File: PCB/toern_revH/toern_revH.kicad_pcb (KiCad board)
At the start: 4 copper layers, 160 x 71 mm, 118 parts, among them IC1 BQ24075TRGTR, J1 AudioJack3_Switch, J10 Conn_01x02, J11 Conn_01x05, J11.5 Conn_01x05, J12 Conn_01x05, J13 Conn_01x05, J14 Conn_01x05, J15 Conn_01x05, J16 Conn_01x02, J17 AudioJack3_Ground, J18 Conn_01x05_Socket, J19 Conn_01x05_Socket, J2 Conn_01x05_Socket, J20 Conn_01x05_Socket, J21 Conn_01x05_Socket, J22 Conn_01x05_Socket, J23 Conn_01x05_Socket, J24 Conn_01x05_Socket, J25 Conn_01x02, J26 Conn_01x02, J3 AudioJack3_Ground, J4 USB_C_Receptacle_USB2.0, J5 AudioJack3_Switch, J6 AudioJack3_Switch, J7 AudioJack3_Switch, J8 Micro_SD_Card, J9 Conn_01x03, U1 SPX3819M5-L-3-3, U13 PAM8403D, U14 74LVC1G17, U15 74AHCT1G125, U2 SPX3819M5-L-1-8, U3 SGTL5000XNBA3, U4 TLP2361V4_E, U5 74LVC2G14, U6 Teensy4.1, U7 SPX3819M5-L-3-3, U8 TPS22918DBVR

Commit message: fixed production files for revH
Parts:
- C32: value 10uF -> 10u
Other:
- board text added: "made in st.pauli by warft_labs V3.0 - 08/26 www.toern.live"
- board text removed: "made in st.pauli by warft_labs V2.1 - 05/26 www.toern.live"

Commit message: added protection for 5-12v clock input as well as 2nd clockout
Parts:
- removed MountingHole5: MountingHole_2.2mm_M2, MountingHole:MountingHole_2.2mm_M2
- added C39: 100nF, Capacitor_SMD:C_0402_1005Metric, F.Cu at (169.1, 37.1)
- added D2: D_Schottky_Dual_Series_ACK, Package_TO_SOT_SMD:SOT-23, F.Cu at (163.3, 30.3)
- added J27: Conn_01x02, Connector_JST:JST_PH_B2B-PH-K_1x02_P2.00mm_Vertical, F.Cu at (185.2, 68.2)
- added R31: 100k, Resistor_SMD:R_0402_1005Metric, F.Cu at (163.3, 38.8)
- added R32: 1k, Resistor_SMD:R_0402_1005Metric, F.Cu at (168.9, 39.4)
- added U16: 74AHCT1G125, Package_TO_SOT_SMD:SOT-23-5, F.Cu at (166.0, 38.9)
- R30: value 10k -> 22k
- moved R29 4.21 mm to (166.6, 31.2), turned to 0 degrees
- moved R30 4.11 mm to (166.5, 29.4), turned to 0 degrees
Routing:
- net Net-(J27-Pin_1): track 0.00 -> 42.2 mm, vias 0 -> 2
- net GND: track 159.9 -> 175.6 mm, vias 165 -> 172
- net 38_CS1_IN1: track 7.12 -> 17.9 mm
- net 35_TX8: track 41.8 -> 50.6 mm, vias 0 -> 2
- net Net-(D2-common): track 5.36 -> 13.0 mm
- net 28_RX7: track 0.00 -> 5.12 mm
- net 41_A17: track 68.5 -> 73.4 mm
- net +5V: track 415.6 -> 419.4 mm, vias 3 -> 4
- net 37_CS: track 20.6 -> 23.5 mm
- net +3.3V: track 375.9 -> 378.6 mm, vias 15 -> 17
- net Net-(R32-Pad2): track 0.00 -> 2.17 mm
- net 34_RX8: track 30.1 -> 31.0 mm
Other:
- board text added: "+ -"
- board text added: "SIDEC-5V"

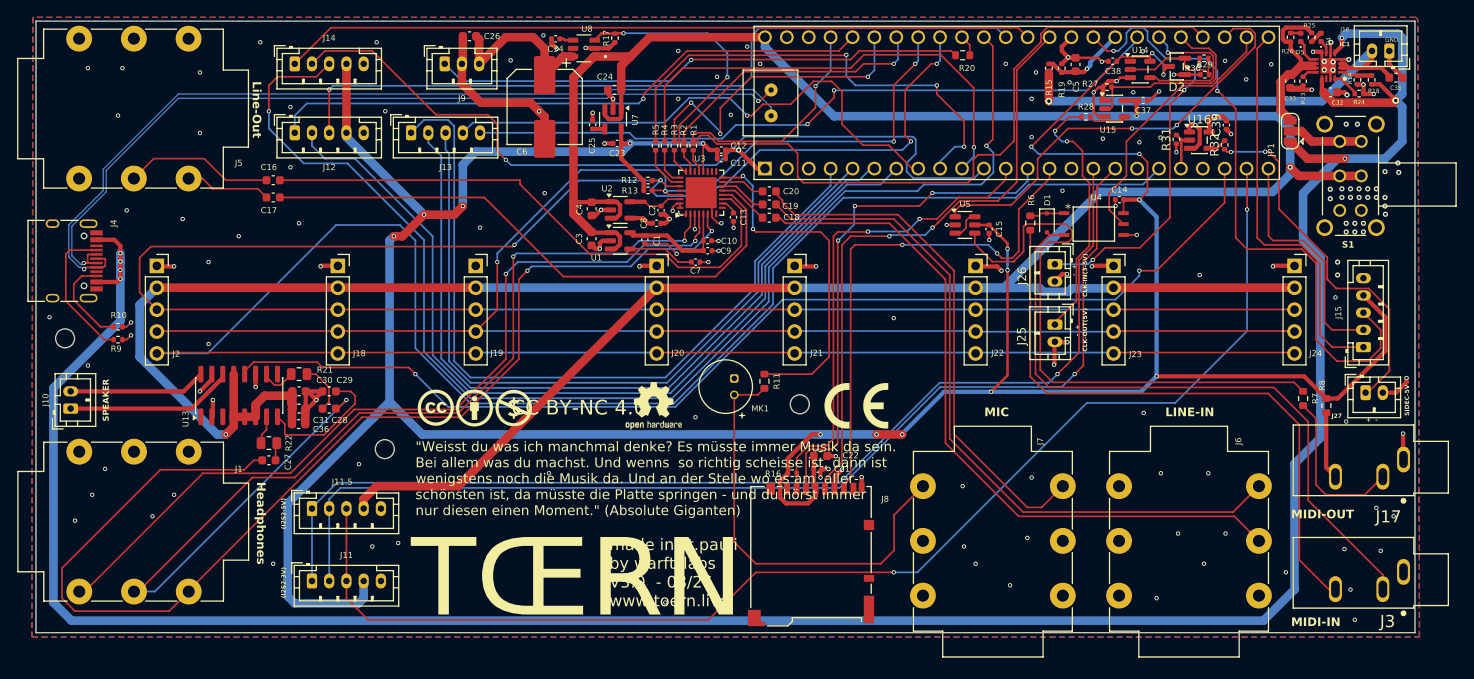
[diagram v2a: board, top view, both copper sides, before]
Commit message: added pogo pins and connectors to pcv revH
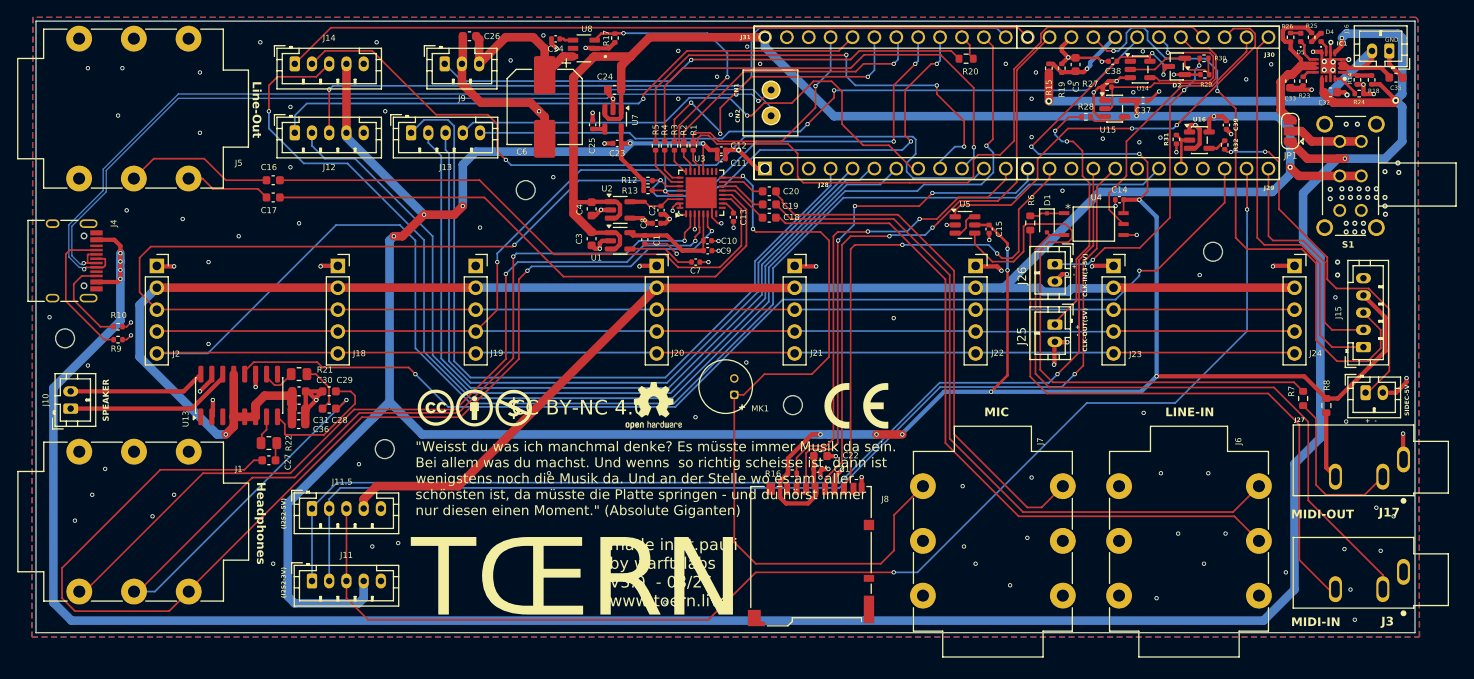
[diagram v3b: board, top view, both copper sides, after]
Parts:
- removed R11: 2.2k, Resistor_SMD:R_0603_1608Metric
- added CN1: YZP0354-20100-01, YZP0354-20100-01:YZP0354-20100-01, F.Cu at (116.3, 33.0)
- added CN2: YZP0354-20100-01, YZP0354-20100-01:YZP0354-20100-01, F.Cu at (116.3, 36.0)
- added J28: 929870-01-12-RA, 3M_929870-01-12-RA:3M_929870-01-12-RA_Assembly, F.Cu at (129.5, 42.1)
- added J29: 929870-01-12-RA, 3M_929870-01-12-RA:3M_929870-01-12-RA_Assembly, F.Cu at (160.0, 42.1)
- added J30: 929870-01-12-RA, 3M_929870-01-12-RA:3M_929870-01-12-RA_Assembly, F.Cu at (160.0, 26.9)
- added J31: 929870-01-12-RA, 3M_929870-01-12-RA:3M_929870-01-12-RA_Assembly, F.Cu at (129.5, 26.9)
- added MountingHole3: MountingHole_2.2mm_M2, MountingHole:MountingHole_2.2mm_M2, F.Cu at (87.8, 44.6)
- added MountingHole5: MountingHole_2.2mm_M2, MountingHole:MountingHole_2.2mm_M2, F.Cu at (167.6, 51.8)
- MK1: footprint Sensor_Audio:POM-2244P-C3310-2-R -> C529951:MIC-TH_BD6.0-P1.90-D0.4-L-FD
- moved MountingHole2 0.81 mm to (118.8, 69.6)
- moved R20 0.57 mm to (138.9, 29.4)
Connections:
- J7 pad TN: Net-(MK1-+) -> MICBIAS
- MK1 pad 1: GND -> MICBIAS
- MK1 pad 2: Net-(MK1-+) -> GND
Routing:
- net MICBIAS: track 40.3 -> 91.0 mm
- net Net-(MK1-+): track 50.1 -> 0.00 mm
- net Net-(J9-Pin_1): track 61.9 -> 62.6 mm
- net GND: vias 172 -> 173
